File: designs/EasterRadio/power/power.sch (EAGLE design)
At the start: 13 parts, among them IC1 MCP73832T-2ACI_OT, IC3 DMP1045U-7, J4 S2B-PH-SM4, J6 PJ-002AH-SMT-TR

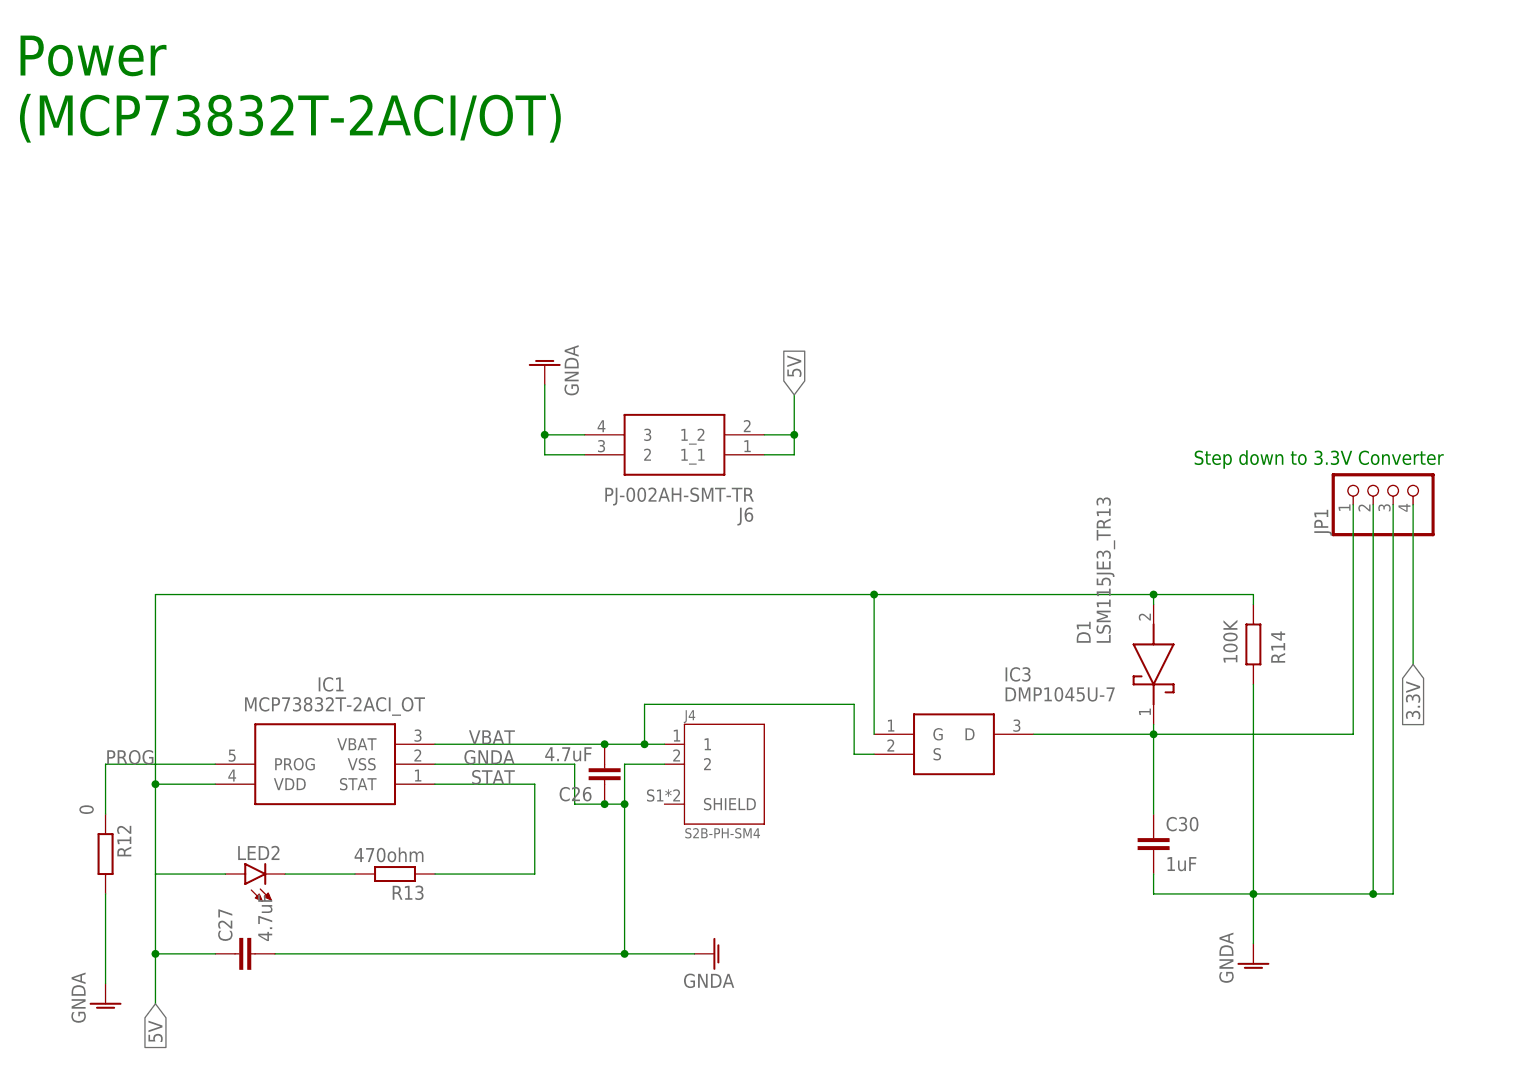
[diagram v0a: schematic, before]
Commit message: changed polarity of power and battery + drain source change imn p channel mosfet
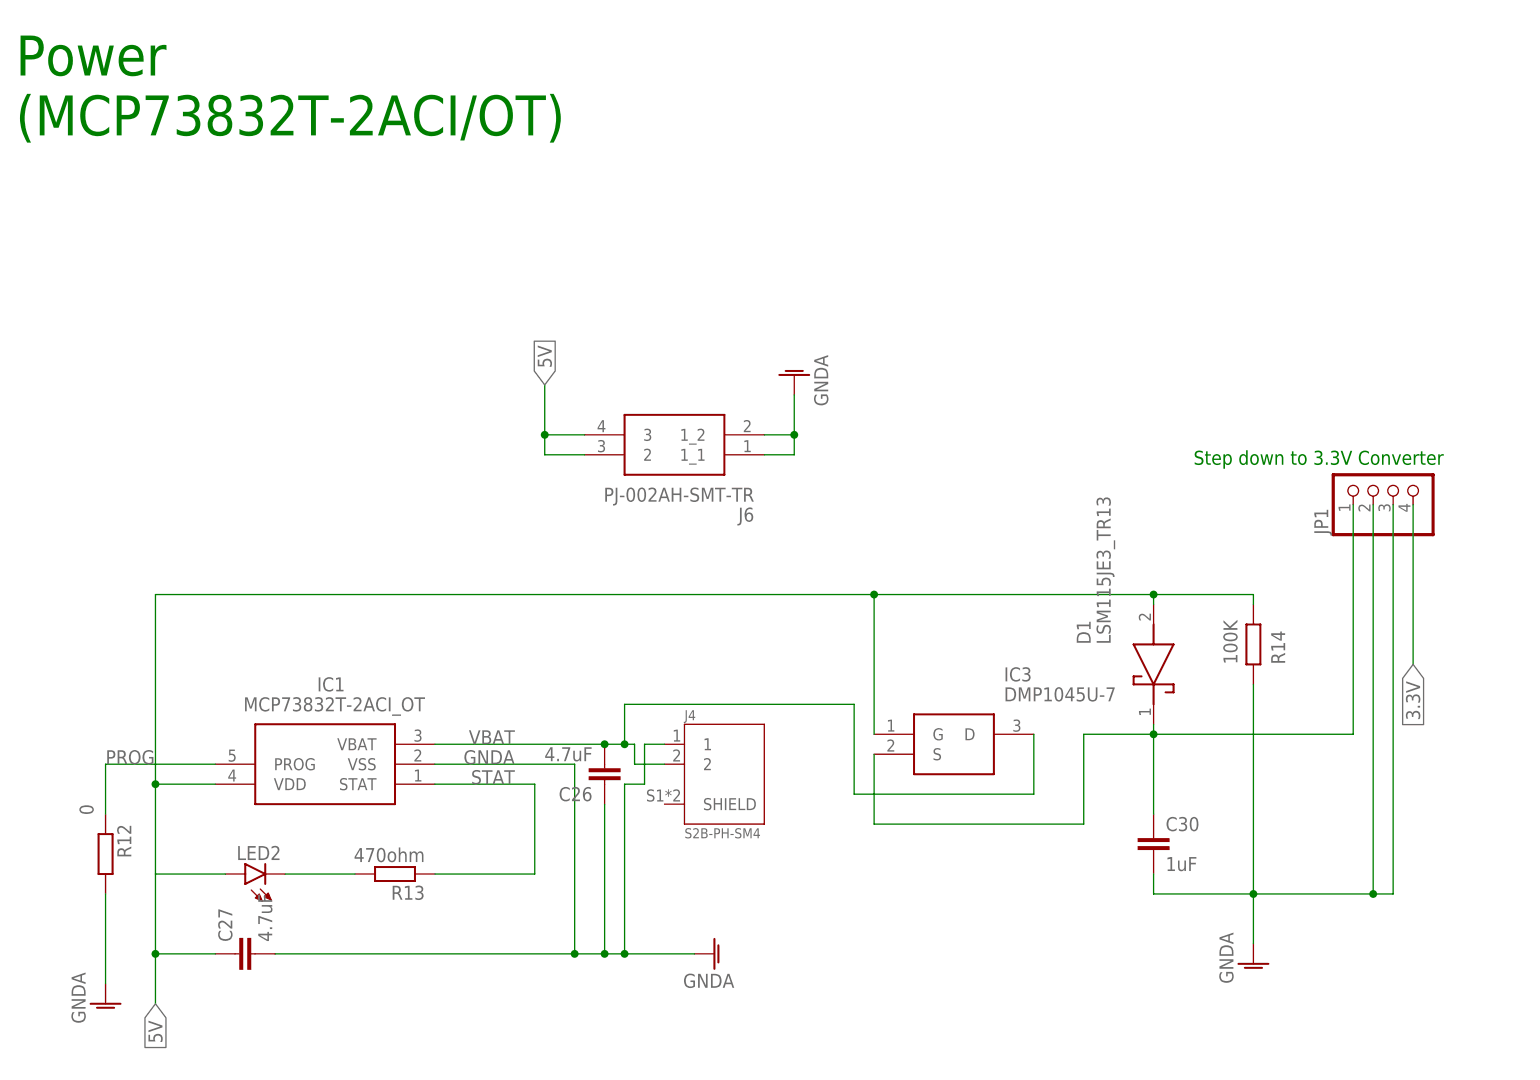
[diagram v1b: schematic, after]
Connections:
- net 5V: now also J6.2, J6.3; no longer J6.1_1, J6.1_2
- net GNDA: now also J4.1, J6.1_1, J6.1_2; no longer J4.2, J6.2, J6.3
- net U_DRAIN: now also IC3.S; no longer IC3.D
- net VBAT: now also IC3.D, J4.2; no longer IC3.S, J4.1

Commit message: changed power board: added comments in schematic and added new LED (to be checked) which is on as soon as charging is done
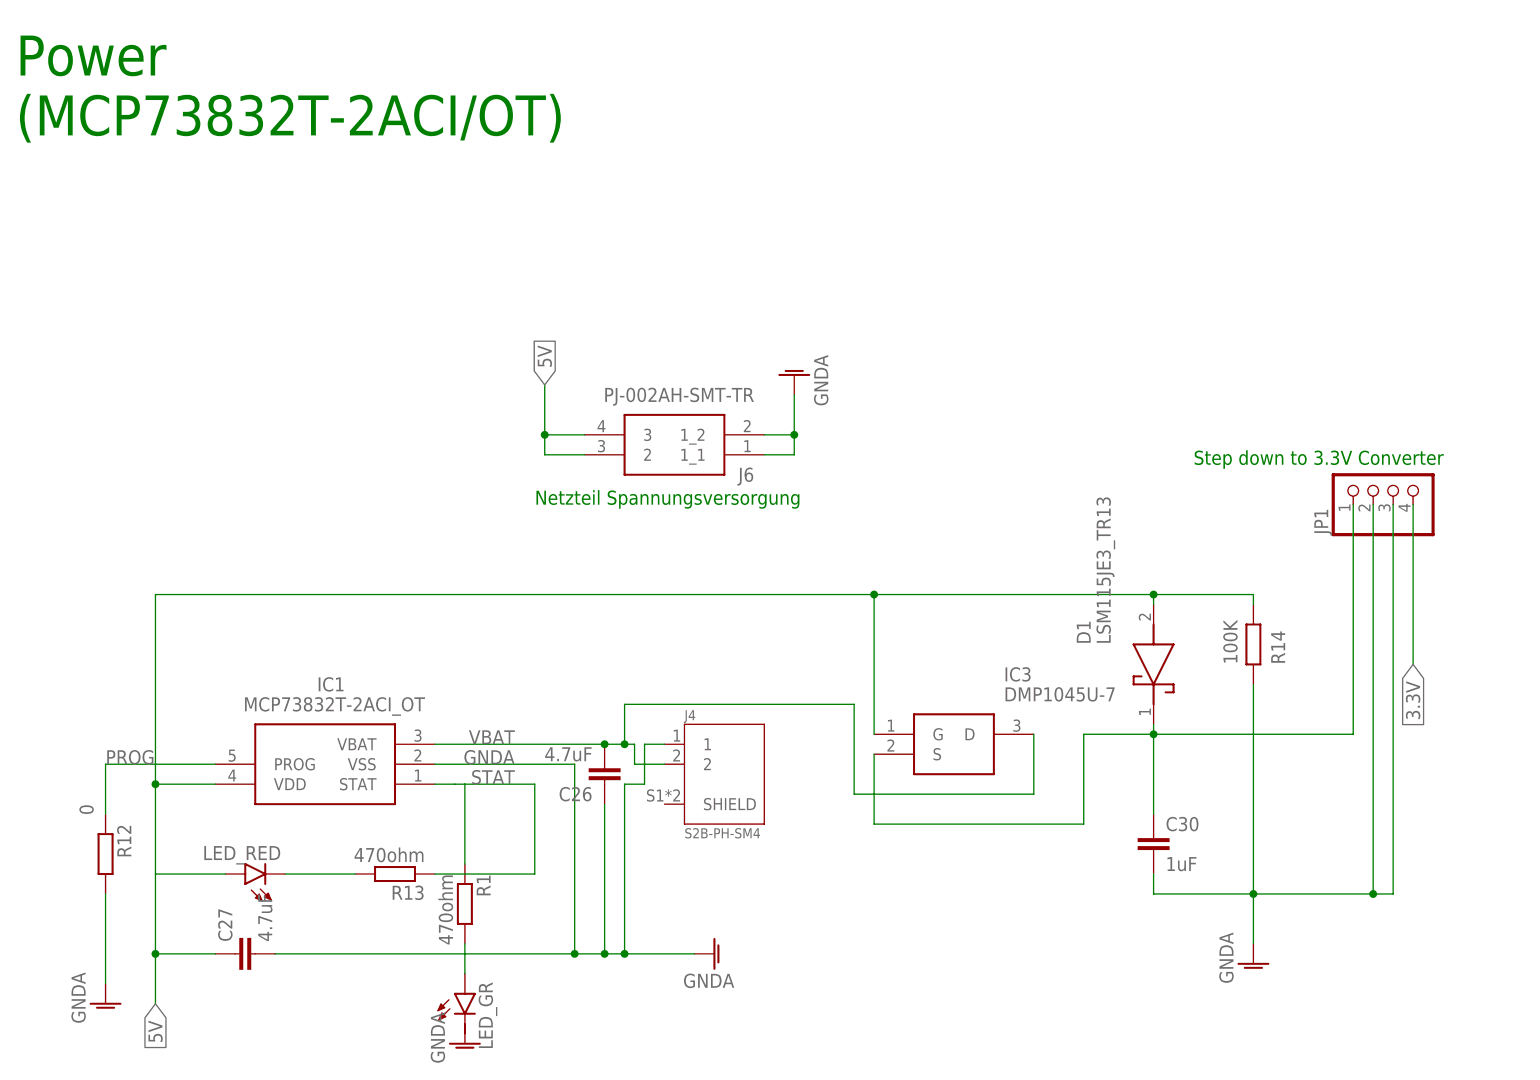
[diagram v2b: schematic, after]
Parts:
- added LED_GR: (no value), CommonParts:LED_1206SMT1206
- added R1: 470ohm, CommonParts:R-EU_1206R1206
- renumbered LED2 to LED_RED
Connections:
- new net N$1: LED_GR.A, R1.2
- net STAT: now also R1.1
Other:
- note added: "Charging Done"
- note added: "Lade-IC STAT = Low --> Battery charging"
- note added: "Netzteil Spannungsversorgung"
- note added: "Shottky diode to prevent current flowing from the battery into the charging power source"
- note added: "pMOSFET runs current when ext. v. source is NOT connected"
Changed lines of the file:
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@@
 <?xml version="1.0" encoding="utf-8"?>
 <!DOCTYPE eagle SYSTEM "eagle.dtd">
-<eagle version="9.6.1">
+<eagle version="9.6.2">
 <drawing>
 <settings>
@@
 <setting verticaltext="up"/>
 </settings>
-<grid distance="0.05" unitdist="inch" unit="inch" style="lines" multiple="1" display="no" altdistance="0.01" altunitdist="inch" altunit="inch"/>
+<grid distance="0.1" unitdist="inch" unit="inch" style="lines" multiple="1" display="no" altdistance="0.01" altunitdist="inch" altunit="inch"/>
 <layers>
 <layer number="1" name="Top" color="4" fill="1" visible="no" active="no"/>
@@
 <part name="GND3" library="supply1" library_urn="urn:adsk.eagle:library:371" deviceset="GNDA" device=""/>
 <part name="R13" library="CommonParts" deviceset="R-EU_1206" device="R1206" package3d_urn="urn:adsk.eagle:package:23540/2" value="470ohm"/>
-<part name="LED2" library="CommonParts" deviceset="LED_1206" device="SMT1206" package3d_urn="urn:adsk.eagle:package:15796/2"/>
+<part name="LED_RED" library="CommonParts" deviceset="LED_1206" device="SMT1206" package3d_urn="urn:adsk.eagle:package:15796/2"/>
 <part name="C27" library="CommonParts" deviceset="C-EU_1206" device="C1206" package3d_urn="urn:adsk.eagle:package:23618/2" value="4.7uF"/>
 <part name="GND4" library="supply1" library_urn="urn:adsk.eagle:library:371" deviceset="GNDA" device=""/>
@@
 <part name="GND6" library="supply1" library_urn="urn:adsk.eagle:library:371" deviceset="GNDA" device=""/>
 <part name="J4" library="CommonParts" deviceset="S2B-PH-SM4" device=""/>
+<part name="LED_GR" library="CommonParts" deviceset="LED_1206" device="SMT1206" package3d_urn="urn:adsk.eagle:package:15796/2"/>
+<part name="R1" library="CommonParts" deviceset="R-EU_1206" device="R1206" package3d_urn="urn:adsk.eagle:package:23540/2" value="470ohm"/>
+<part name="GND1" library="supply1" library_urn="urn:adsk.eagle:library:371" deviceset="GNDA" device=""/>
 </parts>
 <sheets>
@@
 <frame x1="0" y1="0" x2="186.69" y2="118.11" columns="8" rows="5" layer="91"/>
 <text x="149.86" y="78.74" size="1.778" layer="91">Step down to 3.3V Converter</text>
+<text x="35.56" y="30.48" size="1.778" layer="89">Lade-IC
+STAT = Low --&gt;
+Battery charging</text>
+<text x="66.04" y="73.66" size="1.778" layer="91">Netzteil Spannungsversorgung</text>
+<text x="106.68" y="25.4" size="1.778" layer="89">pMOSFET
+runs current when ext.
+v. source is NOT connected</text>
+<text x="137.16" y="38.1" size="1.778" layer="89">Shottky diode
+to prevent current
+flowing from the battery
+into the charging power source</text>
+<text x="63.5" y="7.62" size="1.778" layer="89">Charging Done</text>
 </plain>
 <instances>
@@
 <attribute name="VALUE" x="52.07" y="29.972" size="1.778" layer="96" rot="R180"/>
 </instance>
-<instance part="LED2" gate="G$1" x="29.21" y="26.67" smashed="yes" rot="R90">
+<instance part="LED_RED" gate="G$1" x="29.21" y="26.67" smashed="yes" rot="R90">
 <attribute name="NAME" x="33.782" y="30.226" size="1.778" layer="95" rot="R180"/>
 <attribute name="VALUE" x="33.782" y="32.385" size="1.778" layer="96" rot="R180"/>
@@
 </instance>
 <instance part="J6" gate="G$1" x="95.25" y="80.01" smashed="yes" rot="R180">
-<attribute name="NAME" x="93.98" y="72.39" size="1.778" layer="95" rot="R180" align="center-left"/>
-<attribute name="VALUE" x="93.98" y="74.93" size="1.778" layer="96" rot="R180" align="center-left"/>
+<attribute name="NAME" x="93.98" y="77.47" size="1.778" layer="95" rot="R180" align="center-left"/>
+<attribute name="VALUE" x="93.98" y="87.63" size="1.778" layer="96" rot="R180" align="center-left"/>
 </instance>
 <instance part="JP1" gate="A" x="175.26" y="76.2" smashed="yes" rot="R90">
@@
 <attribute name="NAME" x="85.0871" y="46.23571875" size="1.272509375" layer="95"/>
 <attribute name="VALUE" x="85.08188125" y="31.21731875" size="1.275409375" layer="96"/>
+</instance>
+<instance part="LED_GR" gate="G$1" x="57.15" y="11.43" smashed="yes">
+<attribute name="NAME" x="60.706" y="4.318" size="1.778" layer="95" rot="R90"/>
+<attribute name="VALUE" x="62.865" y="6.858" size="1.778" layer="96" rot="R90"/>
+</instance>
+<instance part="R1" gate="G$1" x="57.15" y="22.86" smashed="yes" rot="R270">
+<attribute name="NAME" x="58.6486" y="26.67" size="1.778" layer="95" rot="R270"/>
+<attribute name="VALUE" x="53.848" y="26.67" size="1.778" layer="96" rot="R270"/>
+</instance>
+<instance part="GND1" gate="1" x="57.15" y="5.08" smashed="yes">
+<attribute name="VALUE" x="54.61" y="2.54" size="1.778" layer="96" rot="R90"/>
 </instance>
 </instances>
@@
 <segment>
 <pinref part="IC1" gate="G$1" pin="STAT"/>
-<wire x1="53.34" y1="38.1" x2="66.04" y2="38.1" width="0.1524" layer="91"/>
+<wire x1="53.34" y1="38.1" x2="55.88" y2="38.1" width="0.1524" layer="91"/>
 <label x="63.5" y="38.1" size="1.778" layer="95" align="bottom-right"/>
 <pinref part="R13" gate="G$1" pin="1"/>
+<wire x1="57.15" y1="38.1" x2="66.04" y2="38.1" width="0.1524" layer="91"/>
 <wire x1="53.34" y1="26.67" x2="66.04" y2="26.67" width="0.1524" layer="91"/>
 <wire x1="66.04" y1="26.67" x2="66.04" y2="38.1" width="0.1524" layer="91"/>
+<pinref part="R1" gate="G$1" pin="1"/>
+<wire x1="57.15" y1="27.94" x2="57.15" y2="38.1" width="0.1524" layer="91"/>
+<wire x1="57.15" y1="38.1" x2="55.88" y2="38.1" width="0.1524" layer="91"/>
 </segment>
 </net>
@@
 <segment>
 <pinref part="R13" gate="G$1" pin="2"/>
-<pinref part="LED2" gate="G$1" pin="C"/>
+<pinref part="LED_RED" gate="G$1" pin="C"/>
 <wire x1="43.18" y1="26.67" x2="34.29" y2="26.67" width="0.1524" layer="91"/>
 </segment>
@@
 <wire x1="144.78" y1="62.23" x2="157.48" y2="62.23" width="0.1524" layer="91"/>
 <wire x1="157.48" y1="62.23" x2="157.48" y2="60.96" width="0.1524" layer="91"/>
-<pinref part="LED2" gate="G$1" pin="A"/>
+<pinref part="LED_RED" gate="G$1" pin="A"/>
 <pinref part="IC1" gate="G$1" pin="VDD"/>
 <wire x1="25.4" y1="38.1" x2="17.78" y2="38.1" width="0.1524" layer="91"/>
@@
 </segment>
 </net>
+<net name="N$1" class="0">
+<segment>
+<pinref part="LED_GR" gate="G$1" pin="A"/>
+<pinref part="R1" gate="G$1" pin="2"/>
+<wire x1="57.15" y1="13.97" x2="57.15" y2="17.78" width="0.1524" layer="91"/>
+</segment>
+</net>
